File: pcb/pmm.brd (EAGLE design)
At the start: 81.6 x 43 mm, 37 parts, among them IC3 STM32F042F4, J1 AUDIO_JACK_3.5MM_PTH, J2 FFC3B07-05-T, SW3 324_SW, SW4 324_SW, U2 USBC_16P, U4 XC6206_DEV

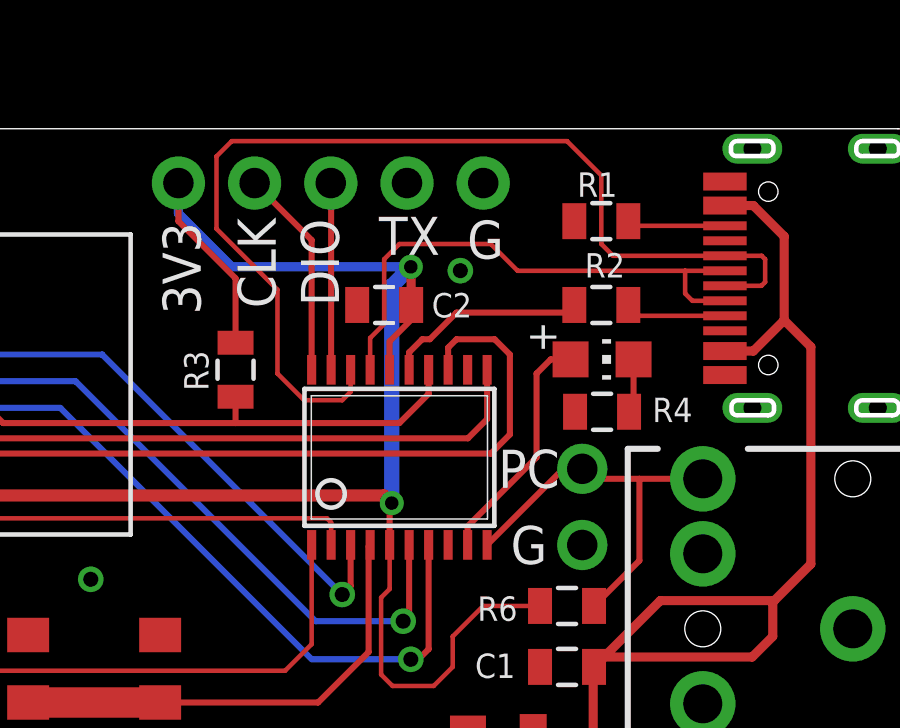
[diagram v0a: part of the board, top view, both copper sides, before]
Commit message: light sensor PCB
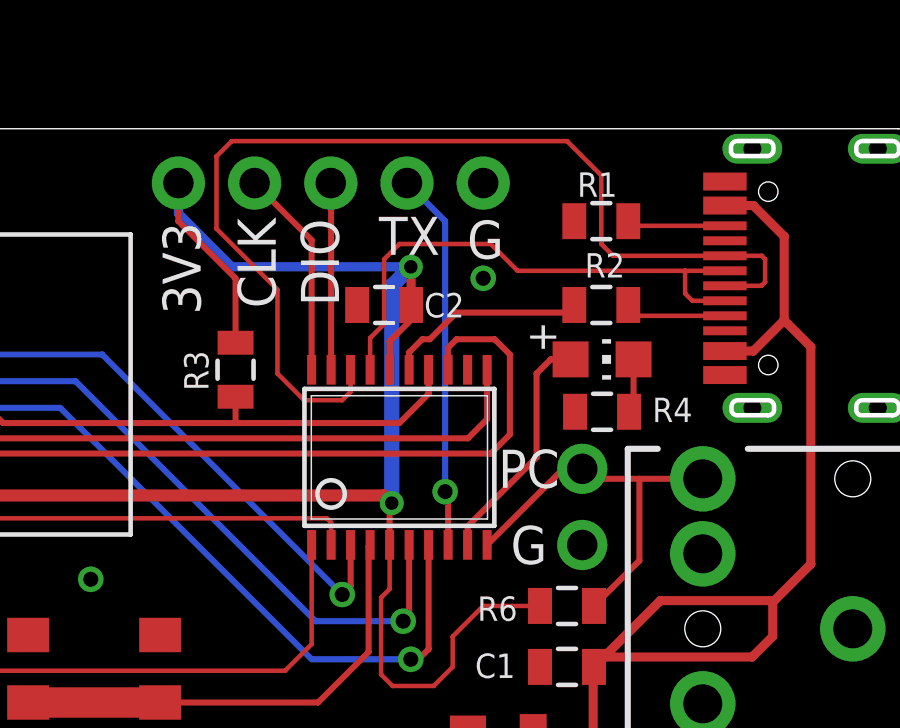
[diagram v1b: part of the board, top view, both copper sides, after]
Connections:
- net UART2_TX: now also U$6.4
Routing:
- net UART2_TX: track 0.00 -> 12.6 mm, vias 0 -> 1
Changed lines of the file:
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@@
 <element name="U4" library="3pos_slide_switch" package="SOT23R_INFINEON" value="XC6206_DEV" x="34.036" y="-22.86" smashed="yes" rot="R270"/>
 <element name="C2" library="clock" package="0805" value="100nF" x="28.067" y="-7.874" smashed="yes">
-<attribute name="NAME" x="30.9918" y="-7.4765" size="0.8128" layer="25" rot="R180"/>
+<attribute name="NAME" x="30.7378" y="-7.4765" size="0.8128" layer="25" rot="R180"/>
 </element>
 <element name="U$12" library="3pos_slide_switch_centered" package="M2_SCREW_FOOT" value="M2_SCREW_DEV" x="6.3" y="15.25" locked="yes" smashed="yes"/>
@@
 <via x="3.556" y="-14.097" extent="1-16" drill="0.5"/>
 <via x="-31.242" y="-4.318" extent="1-16" drill="0.5"/>
-<via x="30.607" y="-6.731" extent="1-16" drill="0.5"/>
+<via x="31.369" y="-6.985" extent="1-16" drill="0.5"/>
 <contactref element="C3" pad="1"/>
 </signal>
@@
 <signal name="UART2_TX">
 <contactref element="IC3" pad="8"/>
+<contactref element="U$6" pad="4"/>
+<wire x1="30.2" y1="-15.8718" x2="30.2" y2="-14.198" width="0.2032" layer="1"/>
+<wire x1="30.2" y1="-14.198" x2="30.099" y2="-14.097" width="0.2032" layer="1"/>
+<via x="30.099" y="-14.097" extent="1-16" drill="0.5"/>
+<wire x1="30.099" y1="-14.097" x2="30.099" y2="-5.08" width="0.2032" layer="16"/>
+<wire x1="30.099" y1="-5.08" x2="28.829" y2="-3.81" width="0.2032" layer="16"/>
 </signal>
 <signal name="OLED_MOSI">

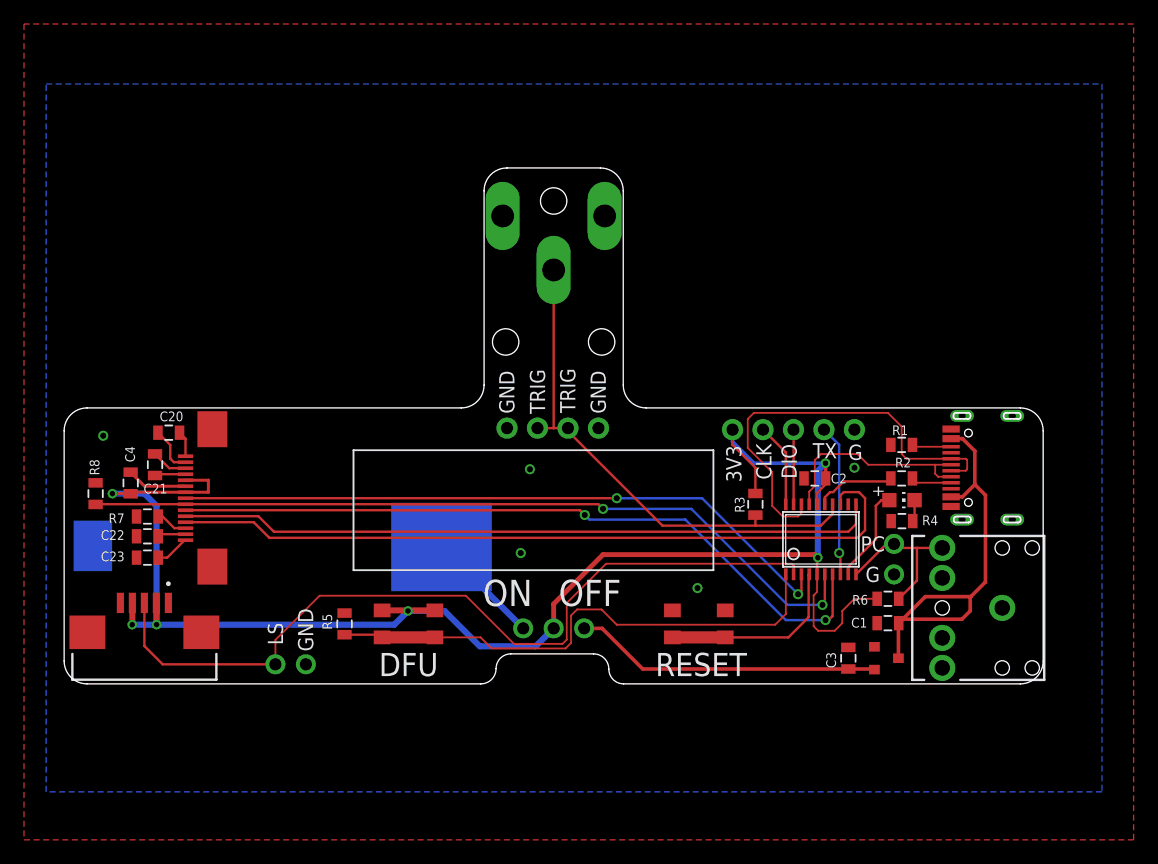
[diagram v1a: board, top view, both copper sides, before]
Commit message: shortened left side
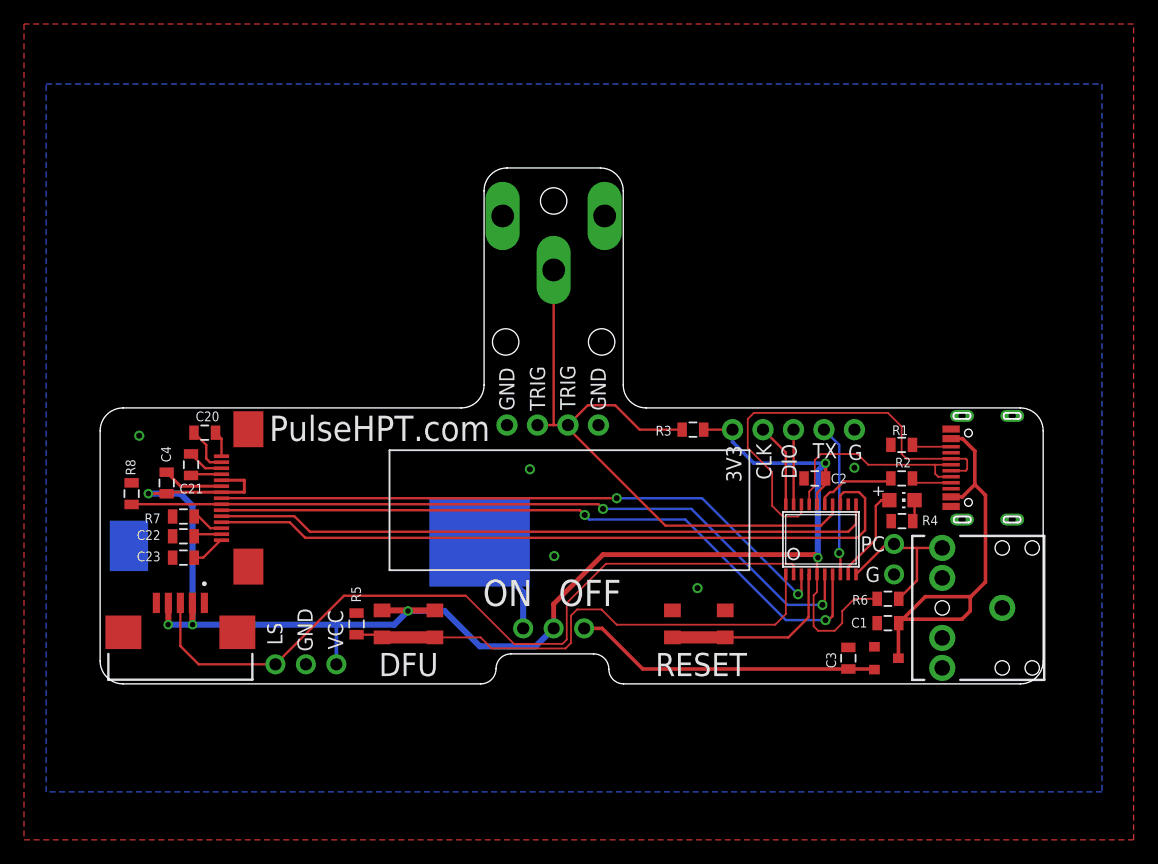
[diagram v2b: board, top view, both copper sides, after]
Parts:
- removed U$9: PINHD1X2, adafruit_changed:1X02
- added JP2: (no value), adafruit_changed:1X03-CLEANBIG
- moved R3 8.11 mm to (17.9, -3.81), turned to 180 degrees
- moved BT1 3.00 mm to (-14.6, -13.5)
- moved C20 3.00 mm to (-22.8, -4.06)
- moved C21 3.00 mm to (-23.9, -6.73)
- moved C22 3.00 mm to (-24.6, -12.7)
- moved C23 3.00 mm to (-24.6, -14.5)
- moved C4 3.00 mm to (-26.0, -8.26)
- moved J2 3.00 mm to (-24.8, -20.7)
- moved R7 3.00 mm to (-24.6, -11.0)
- moved R8 3.00 mm to (-28.9, -9.14)
- moved U1 3.00 mm to (-21.4, -9.53)
- moved R5 1.00 mm to (-10.1, -20.0)
- moved U$7 0.25 mm to (6.22, -3.43)
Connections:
- net +3V3: now also JP2.3
- net GND: now also JP2.2; no longer U$9.2
- net LIGHT_SENSE: now also JP2.1; no longer U$9.1
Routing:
- net N$2: track 43.4 -> 53.4 mm
- net LIGHT_SENSE: track 68.9 -> 64.7 mm
- net +3V3: track 136.9 -> 133.5 mm
- net OLED_MOSI: track 63.2 -> 60.2 mm
- net OLED_SCK: track 58.3 -> 55.3 mm
- net OLED_DC: track 61.3 -> 58.3 mm
- net OLED_CS: track 56.1 -> 53.1 mm
- net OLED_RESET: track 66.7 -> 63.7 mm
- net VBAT: track 9.71 -> 8.47 mm
- net BUTTON2: track 44.1 -> 43.1 mm
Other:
- board size 81.6 x 43 mm -> 78.6 x 43 mm
- board text added: "PulseHPT.com"
- board text added: "VCC"

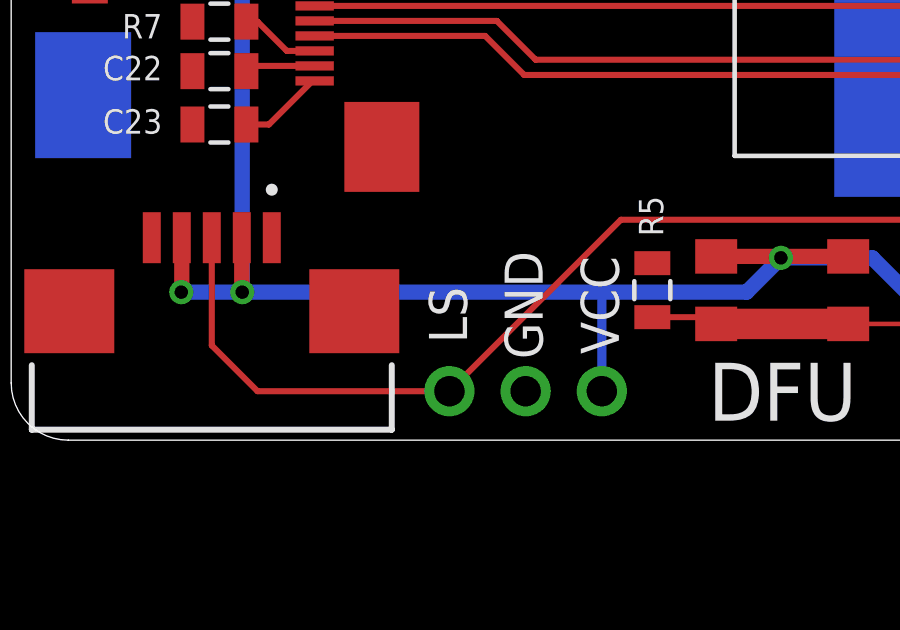
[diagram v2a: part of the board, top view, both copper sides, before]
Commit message: added website
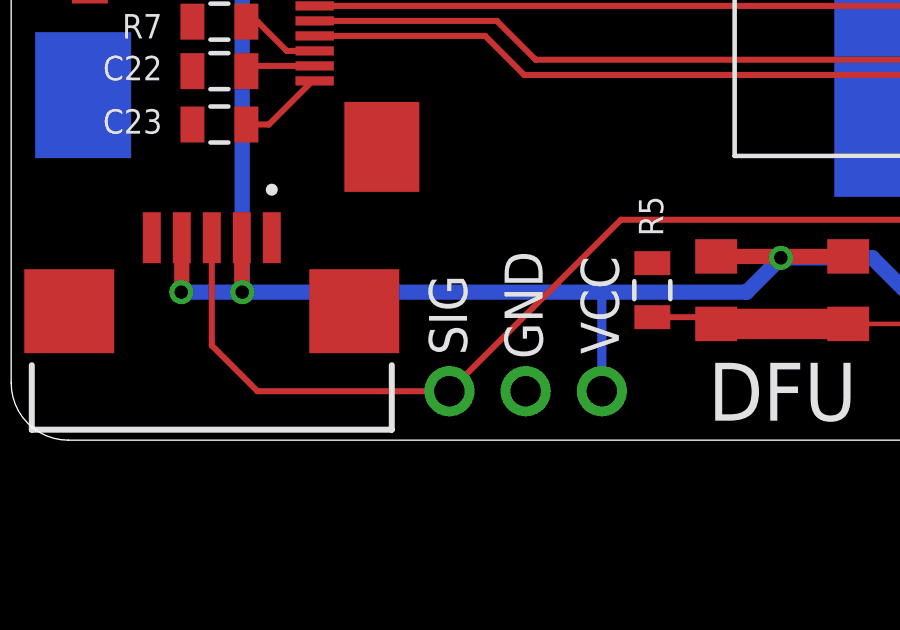
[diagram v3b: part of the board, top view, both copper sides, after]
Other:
- board text added: "PulseHPT.com dekuNukem 2023"
- board text added: "SIG"
- board text removed: "LS"
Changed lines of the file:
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@@
 <text x="32.893" y="-13.335" size="1.27" layer="25" align="center">PC</text>
 <text x="32.893" y="-15.875" size="1.27" layer="25" rot="R180" align="center">G</text>
-<text x="-16.939" y="-20.828" size="1.27" layer="25" rot="R90" align="center">LS</text>
+<text x="-16.939" y="-20.828" size="1.27" layer="25" rot="R90" align="center">SIG</text>
 <text x="-14.4176" y="-20.4982" size="1.27" layer="25" rot="R270" align="center">GND</text>
 <text x="-11.8776" y="-20.4982" size="1.27" layer="25" rot="R270" align="center">VCC</text>
 <text x="-8.2038" y="-3.7016" size="2.1082" layer="25" align="center">PulseHPT.com</text>
+<text x="14.6562" y="-13.6076" size="2.1082" layer="26" rot="MR0" align="center">PulseHPT.com
+dekuNukem 2023</text>
 </plain>
 <attributes>
@@
 </board>
 </drawing>
+<compatibility>
+<note version="6.3" minversion="6.2.2" severity="warning">
+Since Version 6.2.2 text objects can contain more than one line,
+which will not be processed correctly with this version.
+</note>
+</compatibility>
 </eagle>

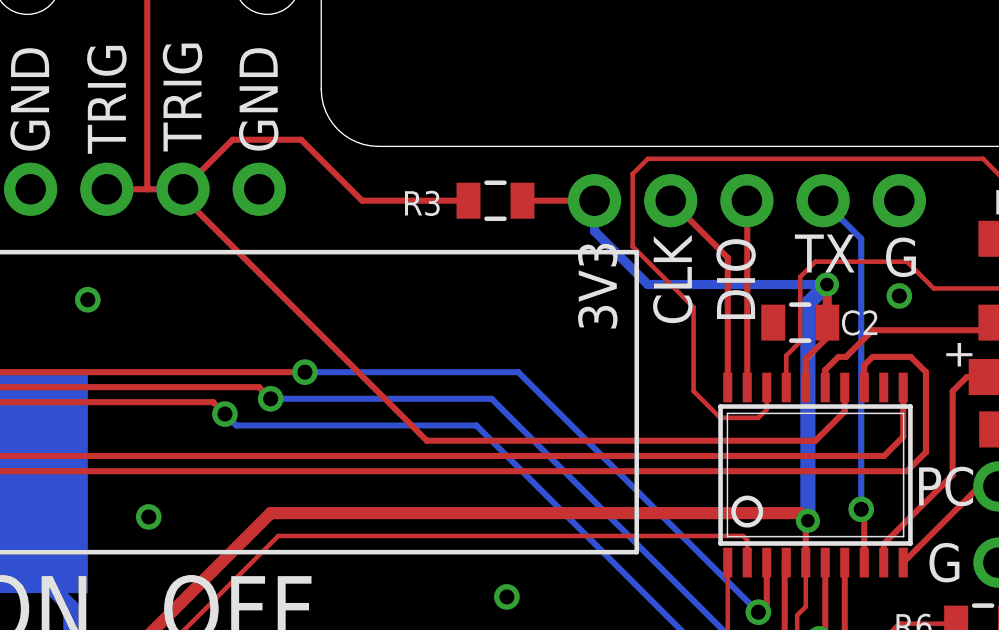
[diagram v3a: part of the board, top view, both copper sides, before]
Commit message: added website
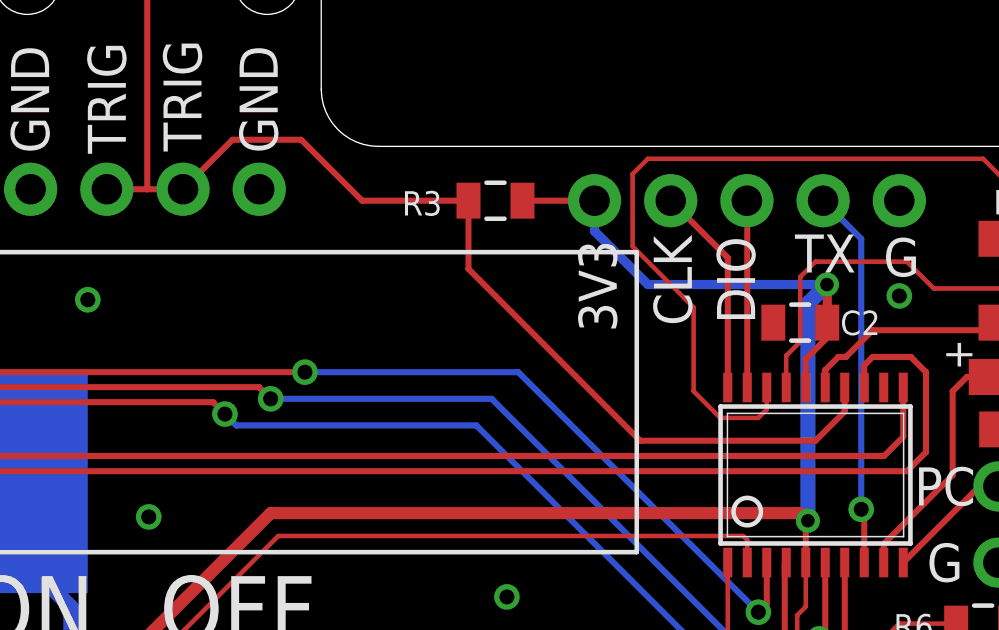
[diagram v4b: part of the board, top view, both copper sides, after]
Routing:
- net N$2: track 53.4 -> 44.9 mm
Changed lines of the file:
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@@
 <layer number="19" name="Unrouted" color="6" fill="1" visible="yes" active="yes"/>
 <layer number="20" name="Dimension" color="24" fill="1" visible="yes" active="yes"/>
-<layer number="21" name="tPlace" color="7" fill="1" visible="yes" active="yes"/>
-<layer number="22" name="bPlace" color="7" fill="1" visible="yes" active="yes"/>
+<layer number="21" name="tPlace" color="7" fill="1" visible="no" active="yes"/>
+<layer number="22" name="bPlace" color="7" fill="1" visible="no" active="yes"/>
 <layer number="23" name="tOrigins" color="15" fill="1" visible="yes" active="yes"/>
 <layer number="24" name="bOrigins" color="15" fill="1" visible="yes" active="yes"/>
-<layer number="25" name="tNames" color="7" fill="1" visible="yes" active="yes"/>
-<layer number="26" name="bNames" color="7" fill="1" visible="yes" active="yes"/>
-<layer number="27" name="tValues" color="7" fill="1" visible="yes" active="yes"/>
-<layer number="28" name="bValues" color="7" fill="1" visible="yes" active="yes"/>
+<layer number="25" name="tNames" color="7" fill="1" visible="no" active="yes"/>
+<layer number="26" name="bNames" color="7" fill="1" visible="no" active="yes"/>
+<layer number="27" name="tValues" color="7" fill="1" visible="no" active="yes"/>
+<layer number="28" name="bValues" color="7" fill="1" visible="no" active="yes"/>
 <layer number="29" name="tStop" color="7" fill="3" visible="no" active="yes"/>
 <layer number="30" name="bStop" color="7" fill="6" visible="no" active="yes"/>
@@
 <layer number="49" name="Reference" color="7" fill="1" visible="no" active="yes"/>
 <layer number="50" name="dxf" color="7" fill="1" visible="no" active="no"/>
-<layer number="51" name="tDocu" color="7" fill="1" visible="yes" active="yes"/>
-<layer number="52" name="bDocu" color="7" fill="1" visible="yes" active="yes"/>
+<layer number="51" name="tDocu" color="7" fill="1" visible="no" active="yes"/>
+<layer number="52" name="bDocu" color="7" fill="1" visible="no" active="yes"/>
 <layer number="53" name="tGND_GNDA" color="7" fill="1" visible="no" active="no"/>
 <layer number="54" name="bGND_GNDA" color="7" fill="1" visible="no" active="no"/>
@@
 <wire x1="6.3" y1="-3.429" x2="7.493" y2="-3.429" width="0.2032" layer="1"/>
 <wire x1="6.3" y1="9.5" x2="6.3" y2="-3.429" width="0.2032" layer="1"/>
-<wire x1="7.493" y1="-3.429" x2="7.493" y2="-3.683" width="0.2032" layer="1"/>
-<wire x1="15.621" y1="-11.811" x2="28.575" y2="-11.811" width="0.2032" layer="1"/>
-<wire x1="7.493" y1="-3.683" x2="15.621" y2="-11.811" width="0.2032" layer="1"/>
 <contactref element="R3" pad="2"/>
 <wire x1="17.007" y1="-3.81" x2="13.462" y2="-3.81" width="0.2032" layer="1"/>
@@
 <wire x1="11.43" y1="-1.778" x2="9.144" y2="-1.778" width="0.2032" layer="1"/>
 <wire x1="9.144" y1="-1.778" x2="7.493" y2="-3.429" width="0.2032" layer="1"/>
+<wire x1="17.007" y1="-3.81" x2="17.007" y2="-6.085" width="0.2032" layer="1"/>
+<wire x1="22.733" y1="-11.811" x2="28.575" y2="-11.811" width="0.2032" layer="1"/>
+<wire x1="17.007" y1="-6.085" x2="22.733" y2="-11.811" width="0.2032" layer="1"/>
 </signal>
 <signal name="LIGHT_SENSE">

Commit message: finishing touches
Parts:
- added TP1, TP2, TP3, TP4, TP5: TPTP12R, testpad:TP12R
- moved R8 0.21 mm to (-29.1, -9.14)
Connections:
- net OLED_CS: now also TP1.TP
- net OLED_DC: now also TP2.TP
- net OLED_MOSI: now also TP4.TP
- net OLED_RESET: now also TP5.TP
- net OLED_SCK: now also TP3.TP
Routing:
- net OLED_RESET: track 63.7 -> 65.5 mm
- net OLED_CS: track 53.1 -> 54.7 mm
- net OLED_MOSI: track 60.2 -> 61.4 mm
- net OLED_DC: track 58.3 -> 59.2 mm
- net OLED_SCK: track 55.3 -> 56.2 mm
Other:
- board text added: "CS"
- board text added: "DC"
- board text added: "MOSI"
- board text added: "ORST"
- board text added: "SCK"
